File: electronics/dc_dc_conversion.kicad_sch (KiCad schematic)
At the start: 10 parts, among them U1 AZ1117-ADJ, U2 AZ1117-ADJ

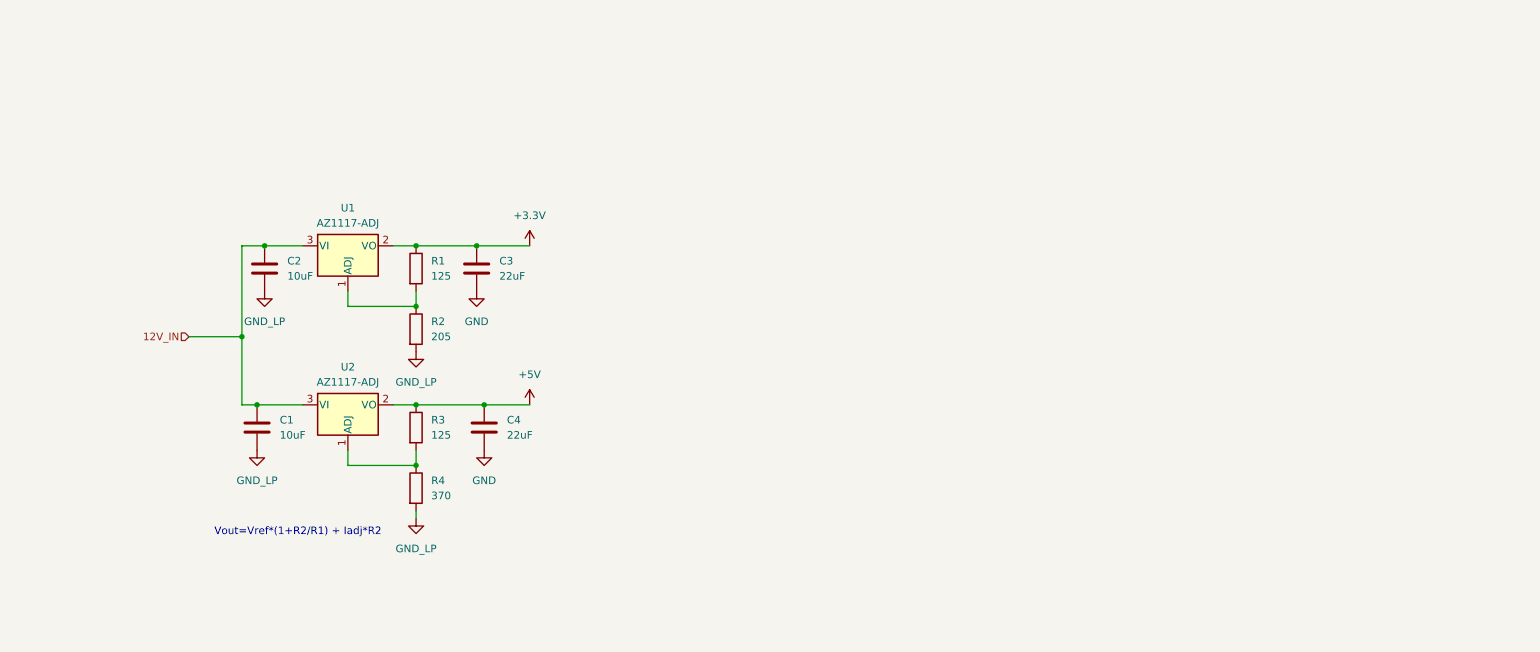
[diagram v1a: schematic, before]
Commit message: start to create BOM and finalising symbol fields
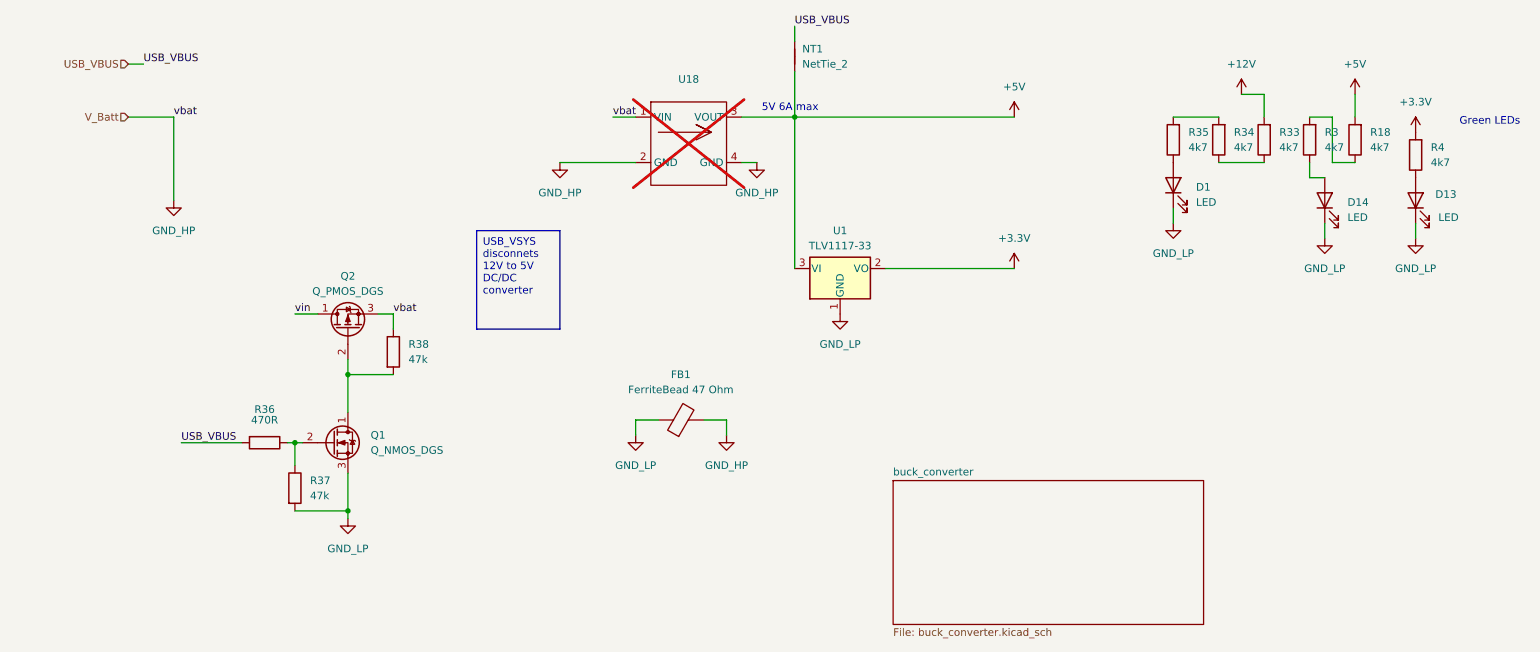
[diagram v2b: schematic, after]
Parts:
- removed C1, C2: 10uF, Capacitor_SMD:C_0805_2012Metric_Pad1.18x1.45mm_HandSolder, symbol Device:C
- removed C3, C4: 22uF, Capacitor_SMD:C_0805_2012Metric_Pad1.18x1.45mm_HandSolder, symbol Device:C
- removed R1: 125, Resistor_SMD:R_0805_2012Metric_Pad1.20x1.40mm_HandSolder, symbol Device:R
- removed R2: 205, Resistor_SMD:R_0805_2012Metric_Pad1.20x1.40mm_HandSolder, symbol Device:R
- removed U1, U2: AZ1117-ADJ, Package_TO_SOT_SMD:SOT-223-3_TabPin2, symbol Regulator_Linear:AZ1117-ADJ
- added D1, D13, D14: LED, LED_SMD:LED_1206_3216Metric, symbol Device:LED
- added FB1: FerriteBead 47 Ohm, Inductor_SMD:L_Walsin_WLFM201609x, symbol Device:FerriteBead
- added NT1: NetTie_2, NetTie:NetTie-2_THT_Pad1.0mm, symbol Device:NetTie_2
- added Q1: Q_NMOS_DGS, Package_TO_SOT_SMD:SOT-323_SC-70, symbol Device:Q_NMOS_DGS
- added Q2: Q_PMOS_DGS, Package_TO_SOT_SMD:SOT-323_SC-70, symbol Device:Q_PMOS_DGS
- added R18, R33, R34, R35: 4k7, Resistor_SMD:R_0805_2012Metric, symbol Device:R
- added R36: 470R, Resistor_SMD:R_0805_2012Metric, symbol Device:R
- added R37, R38: 47k, Resistor_SMD:R_0805_2012Metric, symbol Device:R
- added U1: TLV1117-33, Package_TO_SOT_SMD:SOT-223-3_TabPin2, symbol Regulator_Linear:TLV1117-33
- added U18: ~, HeavyDuty:mini360, symbol HeavyDuty:DC/DC_Buck_Converter
- R3: value 125 -> 4k7; footprint Resistor_SMD:R_0805_2012Metric_Pad1.20x1.40mm_HandSolder -> Resistor_SMD:R_0805_2012Metric
- R4: value 370 -> 4k7; footprint Resistor_SMD:R_0805_2012Metric_Pad1.20x1.40mm_HandSolder -> Resistor_SMD:R_0805_2012Metric
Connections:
- net +3.3V: now also R4.2, U1.2 (VO)
- net +5V: now also NT1.1, R18.2, U1.3 (VI), U18.3 (VOUT); no longer R3.1
- net GND_LP: now also D1.1 (K), D13.1 (K), D14.1 (K), FB1.1, Q1.3 (S), R37.2, U1.1 (GND); no longer R4.2
- net at R3.2: now also R18.1; no longer R4.1
- new net: D14.2 (A), R3.1
- new net: R33.1, R34.1
- new net: D13.2 (A), R4.1
- new net: D1.2 (A), R35.1
- new net: R34.2, R35.2
- new net: Q1.1 (D), Q2.2 (G), R38.2
- new net: Q1.2 (G), R36.1, R37.1
- new net +12V: R33.2
- new net GND_HP: FB1.2, Q2.3 (S), R38.1, U18.1 (VIN), U18.2 (GND), U18.4 (GND)
- new net USB_VBUS: NT1.2, R36.2
- new net vin: Q2.1 (D)
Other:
- added sheet buck_converter (buck_converter.kicad_sch)
- note added: "5V 6A max"
- note added: "Green LEDs"
- note removed: "Vout=Vref*(1+R2/R1) + Iadj*R2"

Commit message: progres on layouting
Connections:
- net GND_HP: no longer Q2.3 (S), R38.1, U18.1 (VIN)
- new net V_Batt: Q2.3 (S), R38.1, U18.1 (VIN)
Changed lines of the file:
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@@
-	(wire
-		(pts
-			(xy 49.53 38.1) (xy 49.53 52.07)
-		)
-		(stroke
-			(width 0)
-			(type default)
-		)
-	)
 	(wire
 		(pts
@@
 	(label "vbat"
 		(at 49.53 38.1 0)
-		(fields_autoplaced yes)
 		(effects
 			(font
@@
 	(label "vin"
 		(at 69.85 71.12 0)
-		(fields_autoplaced yes)
 		(effects
 			(font
@@
 	(label "vbat"
 		(at 86.36 71.12 0)
-		(fields_autoplaced yes)
 		(effects
 			(font
@@
 	(label "USB_VBUS"
 		(at 44.45 29.21 0)
-		(fields_autoplaced yes)
 		(effects
 			(font
@@
 	(label "USB_VBUS"
 		(at 153.67 22.86 0)
-		(fields_autoplaced yes)
 		(effects
 			(font
@@
 	(label "vbat"
 		(at 123.19 38.1 0)
-		(fields_autoplaced yes)
 		(effects
 			(font
@@
 	(label "USB_VBUS"
 		(at 50.8 92.71 0)
-		(fields_autoplaced yes)
 		(effects
 			(font
@@
 		(shape input)
 		(at 41.91 38.1 180)
-		(fields_autoplaced yes)
 		(effects
 			(font
@@
 		(shape input)
 		(at 41.91 29.21 180)
-		(fields_autoplaced yes)
 		(effects
 			(font
@@
 					(unit 1)
 				)
-			)
-		)
-	)
-	(symbol
-		(lib_id "power:GND1")
-		(at 49.53 52.07 0)
-		(unit 1)
-		(exclude_from_sim no)
-		(in_bom yes)
-		(on_board yes)
-		(dnp no)
-		(fields_autoplaced yes)
-		(property "Reference" "#PWR057"
-			(at 49.53 58.42 0)
-			(effects
-				(font
-					(size 1.27 1.27)
-				)
-				(hide yes)
-			)
-		)
-		(property "Value" "GND_HP"
-			(at 49.53 57.15 0)
-			(effects
-				(font
-					(size 1.27 1.27)
-				)
-			)
-		)
-		(property "Footprint" ""
-			(at 49.53 52.07 0)
-			(effects
-				(font
-					(size 1.27 1.27)
-				)
-				(hide yes)
-			)
-		)
-		(property "Datasheet" ""
-			(at 49.53 52.07 0)
-			(effects
-				(font
-					(size 1.27 1.27)
-				)
-				(hide yes)
-			)
-		)
-		(property "Description" "Power symbol creates a global label with name \"GND1\" , ground"
-			(at 49.53 52.07 0)
-			(effects
-				(font
-					(size 1.27 1.27)
-				)
-				(hide yes)
-			)
-		)
-		(pin "1"
-		)
-		(instances
-			(project "electronics"
-				(path "/eeb1234c-eae0-4ac6-a30d-2a978d66d889/04c402f1-b99a-4823-99a0-0c7312782f29/e988bf0b-0303-4560-abbf-9db3a1d13611"
-					(reference "#PWR057")
-					(unit 1)
-				)

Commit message: layouting progress. some 3d models upload
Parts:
- removed NT1: NetTie_2, NetTie:NetTie-2_THT_Pad1.0mm, symbol Device:NetTie_2
- added D15: D_Schottky, Diode_SMD:D_SMA, symbol Device:D_Schottky
- added J25: header, Connector_PinHeader_2.54mm:PinHeader_1x02_P2.54mm_Vertical, symbol Connector_Generic:Conn_01x02
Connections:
- net +5V: now also J25.2 (Pin_2)
- net USB_VBUS: now also D15.1 (K), J25.1 (Pin_1); no longer R36.2
- new net USB_VIN: D15.2 (A), R36.2
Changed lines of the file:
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@@
 	(paper "A4")
+	(junction
+		(at 38.1 85.09)
+		(diameter 0)
+		(color 0 0 0 0)
+	)
 	(junction
 		(at 69.85 92.71)
@@
 	(wire
 		(pts
+			(xy 38.1 92.71) (xy 38.1 85.09)
+		)
+		(stroke
+			(width 0)
+			(type default)
+		)
+	)
+	(wire
+		(pts
 			(xy 242.57 55.88) (xy 242.57 58.42)
 		)
@@
 	(wire
 		(pts
+			(xy 154.94 26.67) (xy 153.67 26.67)
+		)
+		(stroke
+			(width 0)
+			(type default)
+		)
+	)
+	(wire
+		(pts
 			(xy 78.74 81.28) (xy 78.74 87.63)
 		)
@@
 	(wire
 		(pts
-			(xy 41.91 29.21) (xy 44.45 29.21)
+			(xy 34.29 85.09) (xy 38.1 85.09)
 		)
 		(stroke
@@
 	(wire
 		(pts
+			(xy 153.67 29.21) (xy 154.94 29.21)
+		)
+		(stroke
+			(width 0)
+			(type default)
+		)
+	)
+	(wire
+		(pts
 			(xy 68.58 92.71) (xy 69.85 92.71)
 		)
@@
 	(wire
 		(pts
-			(xy 41.91 38.1) (xy 49.53 38.1)
+			(xy 31.75 68.58) (xy 39.37 68.58)
 		)
 		(stroke
@@
 	(wire
 		(pts
-			(xy 153.67 22.86) (xy 153.67 25.4)
+			(xy 153.67 22.86) (xy 153.67 26.67)
 		)
 		(stroke
@@
 	(wire
 		(pts
+			(xy 45.72 85.09) (xy 49.53 85.09)
+		)
+		(stroke
+			(width 0)
+			(type default)
+		)
+	)
+	(wire
+		(pts
+			(xy 38.1 92.71) (xy 60.96 92.71)
+		)
+		(stroke
+			(width 0)
+			(type default)
+		)
+	)
+	(wire
+		(pts
 			(xy 142.24 88.9) (xy 138.43 88.9)
 		)
@@
 	(wire
 		(pts
+			(xy 153.67 29.21) (xy 153.67 38.1)
+		)
+		(stroke
+			(width 0)
+			(type default)
+		)
+	)
+	(wire
+		(pts
 			(xy 69.85 92.71) (xy 69.85 96.52)
 		)
@@
 	(wire
 		(pts
-			(xy 50.8 92.71) (xy 60.96 92.71)
-		)
-		(stroke
-			(width 0)
-			(type default)
-		)
-	)
-	(wire
-		(pts
 			(xy 114.3 45.72) (xy 127 45.72)
 		)
@@
 		(pts
 			(xy 123.19 38.1) (xy 127 38.1)
-		)
-		(stroke
-			(width 0)
-			(type default)
-		)
-	)
-	(wire
-		(pts
-			(xy 153.67 30.48) (xy 153.67 38.1)
 		)
 		(stroke
@@
 	)
 	(label "vbat"
-		(at 49.53 38.1 0)
+		(at 39.37 68.58 0)
+		(fields_autoplaced yes)
 		(effects
 			(font
@@
 	(label "vin"
 		(at 69.85 71.12 0)
+		(fields_autoplaced yes)
 		(effects
 			(font
@@
 		)
 	)
-	(label "vbat"
-		(at 86.36 71.12 0)
+	(label "USB_VBUS"
+		(at 49.53 85.09 0)
+		(fields_autoplaced yes)
 		(effects
 			(font
@@
 		)
 	)
-	(label "USB_VBUS"
-		(at 44.45 29.21 0)
+	(label "vbat"
+		(at 86.36 71.12 0)
+		(fields_autoplaced yes)
 		(effects
 			(font
@@
 	(label "USB_VBUS"
 		(at 153.67 22.86 0)
+		(fields_autoplaced yes)
 		(effects
 			(font
@@
 	(label "vbat"
 		(at 123.19 38.1 0)
+		(fields_autoplaced yes)
 		(effects
 			(font
@@
 		)
 	)
-	(label "USB_VBUS"
-		(at 50.8 92.71 0)
+	(hierarchical_label "V_Batt"
+		(shape input)
+		(at 31.75 68.58 180)
+		(fields_autoplaced yes)
 		(effects
 			(font
 				(size 1.27 1.27)
 			)
-			(justify left bottom)
-		)
-	)
-	(hierarchical_label "V_Batt"
+			(justify right)
+		)
+	)
+	(hierarchical_label "USB_VIN"
 		(shape input)
-		(at 41.91 38.1 180)
+		(at 34.29 85.09 180)
+		(fields_autoplaced yes)
 		(effects
 			(font
@@
 		)
 	)
-	(hierarchical_label "USB_VBUS"
-		(shape input)
-		(at 41.91 29.21 180)
-		(effects
-			(font
-				(size 1.27 1.27)
-			)
-			(justify right)
-		)
-	)
 	(symbol
 		(lib_id "Device:R")
@@
 	)
 	(symbol
+		(lib_id "Connector_Generic:Conn_01x02")
+		(at 160.02 26.67 0)
+		(unit 1)
+		(exclude_from_sim no)
+		(in_bom yes)
+		(on_board yes)
+		(dnp no)
+		(fields_autoplaced yes)
+		(property "Reference" "J25"
+			(at 162.56 26.6699 0)
+			(effects
+				(font
+					(size 1.27 1.27)
+				)
+				(justify left)
+			)
+		)
+		(property "Value" "header"
+			(at 162.56 29.2099 0)
+			(effects
+				(font
+					(size 1.27 1.27)
+				)
+				(justify left)
+			)
+		)
+		(property "Footprint" "Connector_PinHeader_2.54mm:PinHeader_1x02_P2.54mm_Vertical"
+			(at 160.02 26.67 0)
+			(effects
+				(font
+					(size 1.27 1.27)
+				)
+				(hide yes)
+			)
+		)
+		(property "Datasheet" "~"
+			(at 160.02 26.67 0)
+			(effects
+				(font
+					(size 1.27 1.27)
+				)
+				(hide yes)
+			)
+		)
+		(property "Description" "Generic connector, single row, 01x02, script generated (kicad-library-utils/schlib/autogen/connector/)"
+			(at 160.02 26.67 0)
+			(effects
+				(font
+					(size 1.27 1.27)
+				)
+				(hide yes)
+			)
+		)
+		(pin "1"
+		)
+		(pin "2"
+		)
+		(instances
+			(project ""
+				(path "/eeb1234c-eae0-4ac6-a30d-2a978d66d889/04c402f1-b99a-4823-99a0-0c7312782f29/e988bf0b-0303-4560-abbf-9db3a1d13611"
+					(reference "J25")
+					(unit 1)
+				)
+			)
+		)
+	)
+	(symbol
 		(lib_id "power:GND2")
 		(at 217.17 55.88 0)
@@
 	)
 	(symbol
-		(lib_id "Device:NetTie_2")
-		(at 153.67 27.94 90)
-		(unit 1)
-		(exclude_from_sim no)
-		(in_bom no)
-		(on_board yes)
-		(dnp no)
-		(fields_autoplaced yes)
-		(property "Reference" "NT1"
-			(at 154.94 26.6699 90)
-			(effects
-				(font
-					(size 1.27 1.27)
-				)
-				(justify right)
-			)
-		)
-		(property "Value" "NetTie_2"
-			(at 154.94 29.2099 90)
-			(effects
-				(font
-					(size 1.27 1.27)
-				)
-				(justify right)
-			)
-		)
-		(property "Footprint" "NetTie:NetTie-2_THT_Pad1.0mm"
-			(at 153.67 27.94 0)
-			(effects
-				(font
-					(size 1.27 1.27)
-				)
-				(hide yes)
-			)
-		)
-		(property "Datasheet" "~"
-			(at 153.67 27.94 0)
-			(effects
-				(font
-					(size 1.27 1.27)
-				)
-				(hide yes)
-			)
-		)
-		(property "Description" "Net tie, 2 pins"
-			(at 153.67 27.94 0)
-			(effects
-				(font
-					(size 1.27 1.27)
-				)
-				(hide yes)
-			)
-		)
-		(pin "2"
-		)
-		(pin "1"
-		)
-		(instances
-			(project "electronics"
-				(path "/eeb1234c-eae0-4ac6-a30d-2a978d66d889/04c402f1-b99a-4823-99a0-0c7312782f29/e988bf0b-0303-4560-abbf-9db3a1d13611"
-					(reference "NT1")
-					(unit 1)
-				)
-			)
-		)
-	)
-	(symbol
 		(lib_id "Device:R")
 		(at 86.36 77.47 0)
@@
 					(unit 1)
 				)
+			)
+		)
+	)
+	(symbol
+		(lib_id "Device:D_Schottky")
+		(at 41.91 85.09 180)
+		(unit 1)
+		(exclude_from_sim no)
+		(in_bom yes)
+		(on_board yes)
+		(dnp no)
+		(fields_autoplaced yes)
+		(property "Reference" "D15"
+			(at 42.2275 78.74 0)
+			(effects
+				(font
+					(size 1.27 1.27)
+				)
+			)
+		)
+		(property "Value" "D_Schottky"
+			(at 42.2275 81.28 0)
+			(effects
+				(font
+					(size 1.27 1.27)
+				)
+			)
+		)
+		(property "Footprint" "Diode_SMD:D_SMA"
+			(at 41.91 85.09 0)
+			(effects
+				(font
+					(size 1.27 1.27)
+				)
+				(hide yes)
+			)
+		)
+		(property "Datasheet" "~"
+			(at 41.91 85.09 0)
+			(effects
+				(font
+					(size 1.27 1.27)
+				)
+				(hide yes)
+			)
+		)
+		(property "Description" "Schottky diode"
+			(at 41.91 85.09 0)
+			(effects
+				(font
+					(size 1.27 1.27)
+				)
+				(hide yes)
+			)
+		)
+		(pin "1"
+		)
+		(pin "2"
+		)
+		(instances
+			(project "electronics"
+				(path "/eeb1234c-eae0-4ac6-a30d-2a978d66d889/04c402f1-b99a-4823-99a0-0c7312782f29/e988bf0b-0303-4560-abbf-9db3a1d13611"
+					(reference "D15")
+					(unit 1)
+				)
